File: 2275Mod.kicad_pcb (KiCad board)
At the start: 2 copper layers, 121.1 x 57.5 mm, 41 parts, among them IC1 LTV-356T, J1 640388-8, J2 TagConnect_TC2030-MCP, J201 Conn_01x03_Male, K1 40.52.8.024.5000, K2 G5LE-14-CF_DC24, Q200 Q_NPN_Darlington_CBE, Q201 Q_NPN_Darlington_CBE, U1 LM340LAZ-5.0, U2 TCLT1600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

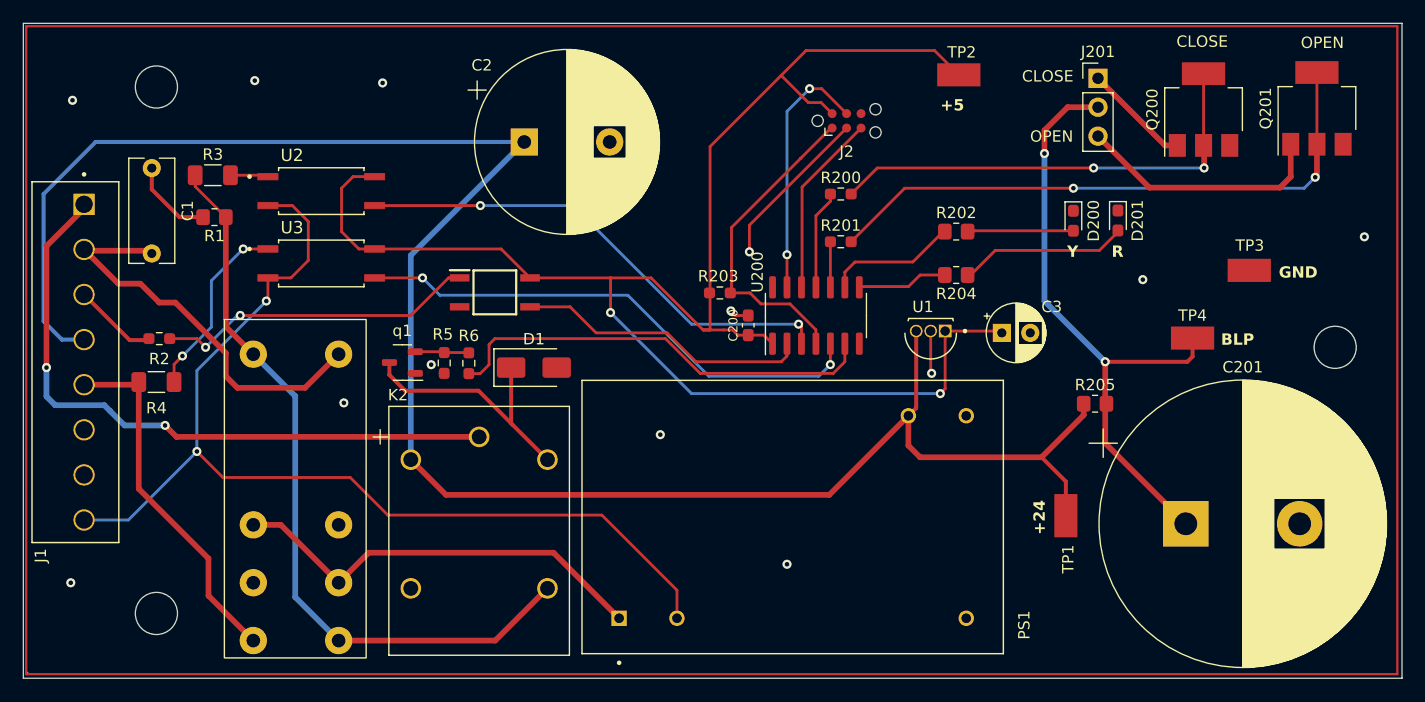
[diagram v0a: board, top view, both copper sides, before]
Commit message: fix k1 wrong foot print re route
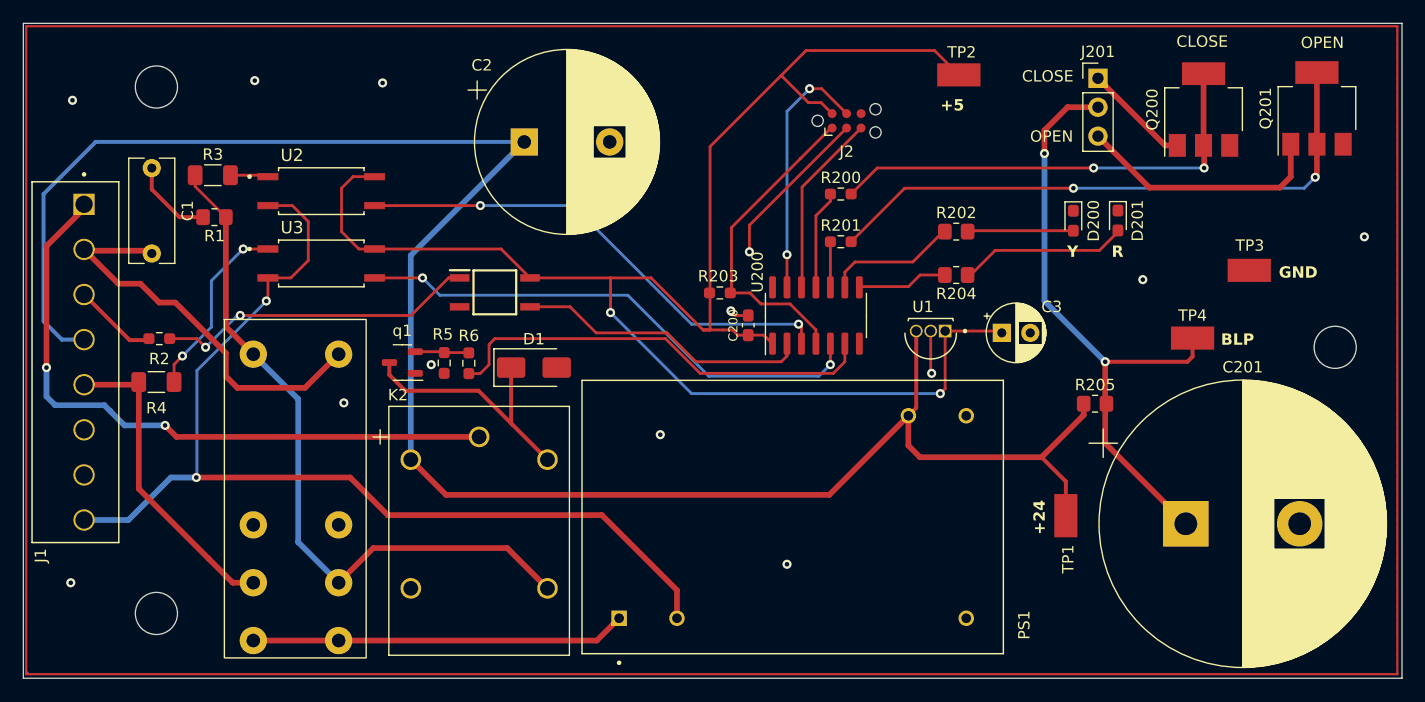
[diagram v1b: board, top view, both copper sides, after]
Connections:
- K1 pad 4: Net-(PS1-VAC_IN(L)) -> /UTIL
- K1 pad 5: /UTIL -> /VAC_IN
- K1 pad 6: Net-(PS1-VAC_IN(L)) -> unconnected-(K1-Pad6)
- K1 pad 7: unconnected-(K1-Pad7) -> /G_L1
- K1 pad 8: /G_L1 -> /VAC_IN
- PS1 pad 1: Net-(PS1-VAC_IN(L)) -> /VAC_IN
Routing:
- net Net-(PS1-VAC_IN(L)): track 37.7 -> 0.00 mm
- net /VAC_IN: track 0.00 -> 32.9 mm
- net /UTIL: track 66.3 -> 62.1 mm
- net /G_L1: track 31.8 -> 27.7 mm
